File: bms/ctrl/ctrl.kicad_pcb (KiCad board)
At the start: 2 copper layers, 1 part

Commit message: BMS stuff update
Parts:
- removed the REF** at (111.9, 82.9)
- added C1: CP_1µ_100V_0805, Resistor_SMD:R_1210_3225Metric, F.Cu at (67.2, 93.3)
- added C2: CP_1µ_100V_0805, Resistor_SMD:R_1210_3225Metric, F.Cu at (67.2, 112.0)
- added C3: CP_330µ_100V_1210, localstuff:CP_Elec_19x19, F.Cu at (55.2, 104.5)
- added C4: 100nF, Capacitor_SMD:C_0603_1608Metric, F.Cu at (103.9, 106.1)
- added C5: CP_100n_50V_0603, Capacitor_SMD:C_0603_1608Metric, F.Cu at (67.0, 115.5)
- added C6: CP_100n_50V_0603, Capacitor_SMD:C_0603_1608Metric, F.Cu at (67.1, 117.4)
- added C7: CP_100n_50V_0603, Capacitor_SMD:C_0603_1608Metric, F.Cu at (67.0, 119.3)
- added C8: CP_10µ_16V_0603, Capacitor_SMD:C_0603_1608Metric, F.Cu at (108.3, 116.8)
- added D1: D_TVS_70V, localstuff:SOD-123FL, F.Cu at (66.9, 98.7)
- added D2: 1N4148, Diode_SMD:D_SOD-123, F.Cu at (105.8, 96.2)
- added D3: D_Schottky, Diode_SMD:D_SOD-123, F.Cu at (68.0, 127.2)
- added D4: D_Zener_3V3, Diode_SMD:D_SOD-123, F.Cu at (68.0, 121.5)
- added D5: 1N4148, Diode_SMD:D_SOD-123, F.Cu at (100.6, 90.5)
- added D6: 1N4148, Diode_SMD:D_SOD-123, F.Cu at (106.9, 91.0)
- added D7: 1N4148, Diode_SMD:D_SOD-123, F.Cu at (104.3, 82.3)
- added F1: Polyfuse 100V, Diode_SMD:D_SMA, F.Cu at (69.2, 104.2)
- added J1: Conn_01x02_Female, localstuff:Conn_P5.0mm_2_Lumberg, F.Cu at (48.0, 132.6)
- added J10: Conn_LEM_3, Connector_JST:JST_PH_B5B-PH-K_1x05_P2.00mm_Vertical, F.Cu at (76.6, 74.0)
- added J11: Conn_01x02_Female, Connector_PinHeader_2.54mm:PinHeader_1x02_P2.54mm_Vertical, F.Cu at (100.9, 73.6)
- added J12: Conn_01x04, Connector_PinHeader_2.54mm:PinHeader_1x04_P2.54mm_Vertical, F.Cu at (61.8, 131.0)
- added J2: Conn_01x02_Female, localstuff:Conn_P5.0mm_2_Lumberg, F.Cu at (95.5, 75.5)
- added J3: ScrewTerminal, Connector_PinHeader_2.54mm:PinHeader_1x04_P2.54mm_Vertical, F.Cu at (108.9, 73.6)
- added J4: Conn_01x06, Connector_PinHeader_2.54mm:PinHeader_1x06_P2.54mm_Vertical, F.Cu at (68.0, 86.9)
- added J5: Conn_01x04, Connector_PinHeader_2.54mm:PinHeader_1x04_P2.54mm_Vertical, F.Cu at (72.1, 74.2)
- added J6: Conn_LEM_5, Connector_JST:JST_PH_B4B-PH-K_1x04_P2.00mm_Vertical, F.Cu at (78.0, 80.2)
- added J7: Conn_01x02_Male, Connector_PinHeader_2.54mm:PinHeader_1x02_P2.54mm_Vertical, F.Cu at (64.1, 74.2)
- added J8: Conn_01x02_Female, Connector_PinHeader_2.54mm:PinHeader_1x02_P2.54mm_Vertical, F.Cu at (104.9, 73.6)
- added J9: Conn_01x03, localstuff:Conn_P5.0mm_3_Lumberg, F.Cu at (58.6, 75.1)
- added JP1: SolderJumper_3_Bridged12, Jumper:SolderJumper-3_P1.3mm_Open_Pad1.0x1.5mm, B.Cu at (109.7, 121.9)
- added JP2: SolderJumper_3_Bridged12, Jumper:SolderJumper-3_P1.3mm_Open_Pad1.0x1.5mm, B.Cu at (107.2, 121.9)
- added JP3: SolderJumper_3_Bridged12, Jumper:SolderJumper-3_P1.3mm_Open_Pad1.0x1.5mm, B.Cu at (102.2, 121.9)
- added JP4: SolderJumper_3_Bridged12, Jumper:SolderJumper-3_P1.3mm_Open_Pad1.0x1.5mm, B.Cu at (104.7, 121.9)
- added JP5: SolderJumper_3_Bridged12, Jumper:SolderJumper-3_P1.3mm_Open_Pad1.0x1.5mm, B.Cu at (99.7, 121.9)
- added JP6: OptTermination, Jumper:SolderJumper-2_P1.3mm_Open_RoundedPad1.0x1.5mm, B.Cu at (101.0, 110.0)
- added JP7: CANBUS Volt Select, Jumper:SolderJumper-3_P1.3mm_Bridged12_RoundedPad1.0x1.5mm, B.Cu at (101.1, 112.7)
- added JP8: Jumper_2_Open, Connector_PinHeader_2.54mm:PinHeader_1x02_P2.54mm_Vertical, F.Cu at (72.0, 88.8)
- added Q1: DMN2058U-7, Package_TO_SOT_SMD:SOT-23, F.Cu at (102.5, 100.5)
- added Q2: XP221P0501TR-G, Package_TO_SOT_SMD:SOT-23, F.Cu at (102.5, 95.5)
- added Q3: DMN2058U-7, Package_TO_SOT_SMD:SOT-23, F.Cu at (109.0, 100.7)
- added Q4: XP221P0501TR-G, Package_TO_SOT_SMD:SOT-23, F.Cu at (109.0, 95.5)
- added Q5: DMN2058U-7, Package_TO_SOT_SMD:SOT-23, F.Cu at (101.5, 87.3)
- added Q6: DMN2058U-7, Package_TO_SOT_SMD:SOT-23, F.Cu at (108.7, 87.9)
- added R1: R_220_0603, Resistor_SMD:R_0603_1608Metric, F.Cu at (110.0, 122.8)
- added R10: R_10k_0603, Resistor_SMD:R_0603_1608Metric, F.Cu at (71.3, 115.1)
- added R11: R_1M_0603, Resistor_SMD:R_0603_1608Metric, F.Cu at (98.7, 87.4)
- added R12: R_120_0603, Resistor_SMD:R_0603_1608Metric, F.Cu at (66.8, 89.8)
- added R13: R_1M_0603, Resistor_SMD:R_0603_1608Metric, F.Cu at (106.0, 88.0)
- added R2: R_2k2_0603, Resistor_SMD:R_0603_1608Metric, F.Cu at (99.8, 122.5)
- added R3: R_1M_0603, Resistor_SMD:R_0603_1608Metric, F.Cu at (99.7, 100.3)
- added R4: R_1M_0603, Resistor_SMD:R_0603_1608Metric, F.Cu at (102.4, 98.0)
- added R5: R_1M_0603, Resistor_SMD:R_0603_1608Metric, F.Cu at (106.1, 100.5)
- added R6: R_1M_0603, Resistor_SMD:R_0603_1608Metric, F.Cu at (109.4, 98.1)
- added R7: 120R, Resistor_SMD:R_0805_2012Metric, F.Cu at (103.8, 109.5)
- added R8: R_750k_0603, Resistor_SMD:R_0603_1608Metric, F.Cu at (67.2, 125.1)
- added R9: R_36k_0603_1, Resistor_SMD:R_0603_1608Metric, F.Cu at (67.2, 123.5)
- added REF**: OSHW-Logo2_9.8x8mm_Copper, Symbol:OSHW-Logo2_9.8x8mm_Copper, B.Cu at (82.8, 126.2)
- added REF**: OSHW-Logo2_9.8x8mm_SilkScreen, Symbol:OSHW-Logo2_9.8x8mm_SilkScreen, B.Cu at (82.8, 126.2)
- added RX1: Conn_01x02_Male, Connector_JST:JST_PH_S2B-PH-K_1x02_P2.00mm_Horizontal, F.Cu at (107.5, 129.6)
- added TP1: TestPoint, TestPoint:TestPoint_Pad_D1.5mm, F.Cu at (71.1, 111.5)
- added TX1: Conn_01x02_Male, Connector_JST:JST_PH_S2B-PH-K_1x02_P2.00mm_Horizontal, F.Cu at (100.4, 129.5)
- added U1: STH05_5V, localstuff:STH05, F.Cu at (53.8, 88.0)
- added U2: STH05_12, localstuff:STH05, F.Cu at (54.2, 120.9)
- added U3: VOS618A, Package_SO:SOP-4_4.4x2.6mm_P1.27mm, F.Cu at (104.8, 122.6)
- added U4: SN65HVD75DR, Package_SO:SOIC-8_3.9x4.9mm_P1.27mm, F.Cu at (107.7, 108.2)
- added U5: Pico, pico:RPi_Pico_SMD_TH, F.Cu at (85.9, 110.4)
- added U6: SN65HVD1050D, Package_SO:SOIC-8_3.9x4.9mm_P1.27mm, F.Cu at (103.7, 116.9)
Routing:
- net GND: track 0.00 -> 386.3 mm, vias 0 -> 27
- net +5V: track 0.00 -> 173.5 mm, vias 0 -> 9
- net +3V3: track 0.00 -> 153.3 mm, vias 0 -> 8
- net +12V: track 0.00 -> 147.4 mm, vias 0 -> 11
- net Net-(J9-Pin_1): track 0.00 -> 85.5 mm, vias 0 -> 3
- net VBAT: track 0.00 -> 85.2 mm, vias 0 -> 7
- net Net-(J9-Pin_2): track 0.00 -> 83.6 mm, vias 0 -> 5
- net ADC_BAT_I: track 0.00 -> 69.1 mm, vias 0 -> 2
- net RESET: track 0.00 -> 64.4 mm, vias 0 -> 3
- net RELAY2: track 0.00 -> 63.3 mm, vias 0 -> 2
- net RELAY1: track 0.00 -> 62.3 mm, vias 0 -> 2
- net ADC_REF_I: track 0.00 -> 59.6 mm, vias 0 -> 2
- net Net-(J3-Pin_2): track 0.00 -> 53.2 mm, vias 0 -> 5
- net I2C0_SDA: track 0.00 -> 42.5 mm, vias 0 -> 2
- net Net-(J3-Pin_3): track 0.00 -> 41.7 mm, vias 0 -> 5
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- added copper zone on B.Cu, net GND
- added copper zone on F.Cu, net GND
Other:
- board outline added: 68.8 x 65 mm
- board text added: "+"
- board text added: "+ - R Combo"
- board text added: "-"
- board text added: "12"
- board text added: "5v CAN 3.3v"
- board text added: "CAN"
- board text added: "GND"
- board text added: "GND L H"
- board text added: "MoaT comm"
- board text added: "MoaT/diyBMS battery controller V 1.0"
- board text added: "R1"
- board text added: "R2"
- board text added: "RS485"
- board text added: "RS485 term"
- board text added: "RX"
- board text added: "TX"
- board text added: "diyBMS comm"

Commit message: minor fixup
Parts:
- turned R7 to 90 degrees
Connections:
- R7 pad 1: Net-(J3-Pin_3) -> Net-(JP6-B)
- R7 pad 2: Net-(JP6-B) -> Net-(J3-Pin_3)
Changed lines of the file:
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@@
   )
   (footprint "Resistor_SMD:R_0805_2012Metric" (layer "F.Cu")
-    (at 103.8 109.4575 -90)
+    (at 103.8 109.4575 90)
     (descr "Resistor SMD 0805 (2012 Metric), square (rectangular) end terminal, IPC_7351 nominal, (Body size source: IPC-SM-782 page 72, https://www.pcb-3d.com/wordpress/wp-content/uploads/ipc-sm-782a_amendment_1_and_2.pdf), generated with kicad-footprint-generator")
     (tags "resistor")
@@
     (property "ki_keywords" "R res resistor")
     (attr smd)
-    (fp_text reference "R7" (at -0.26 1.82 90) (layer "F.SilkS")
+    (fp_text reference "R7" (at 1.2575 -1.4 90) (layer "F.SilkS")
         (effects (font (size 1 1) (thickness 0.15)))
     )
@@
     (fp_line (start 1 0.625) (end -1 0.625)
       (stroke (width 0.1) (type solid)) (layer "F.Fab"))
-    (pad "1" smd roundrect (at -0.9125 0 270) (size 1.025 1.4) (layers "F.Cu" "F.Paste" "F.Mask") (roundrect_rratio 0.243902439)
+    (pad "1" smd roundrect (at -0.9125 0 90) (size 1.025 1.4) (layers "F.Cu" "F.Paste" "F.Mask") (roundrect_rratio 0.243902439)
+      (net 29 "Net-(JP6-B)") (pintype "passive"))
+    (pad "2" smd roundrect (at 0.9125 0 90) (size 1.025 1.4) (layers "F.Cu" "F.Paste" "F.Mask") (roundrect_rratio 0.243902439)
       (net 66 "Net-(J3-Pin_3)") (pintype "passive"))
-    (pad "2" smd roundrect (at 0.9125 0 270) (size 1.025 1.4) (layers "F.Cu" "F.Paste" "F.Mask") (roundrect_rratio 0.243902439)
-      (net 29 "Net-(JP6-B)") (pintype "passive"))
     (model "${KICAD6_3DMODEL_DIR}/Resistor_SMD.3dshapes/R_0805_2012Metric.wrl"
       (offset (xyz 0 0 0))

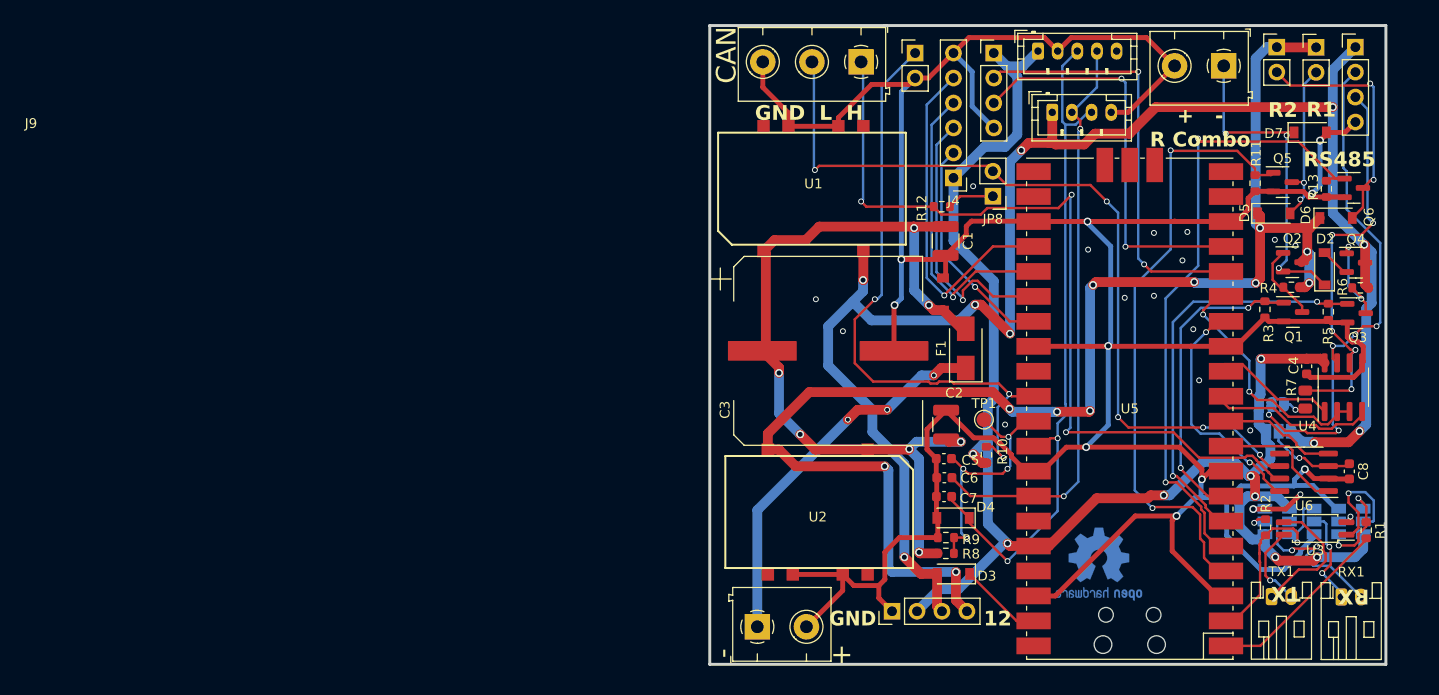
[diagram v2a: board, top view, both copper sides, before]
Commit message: Added two more config jumpers
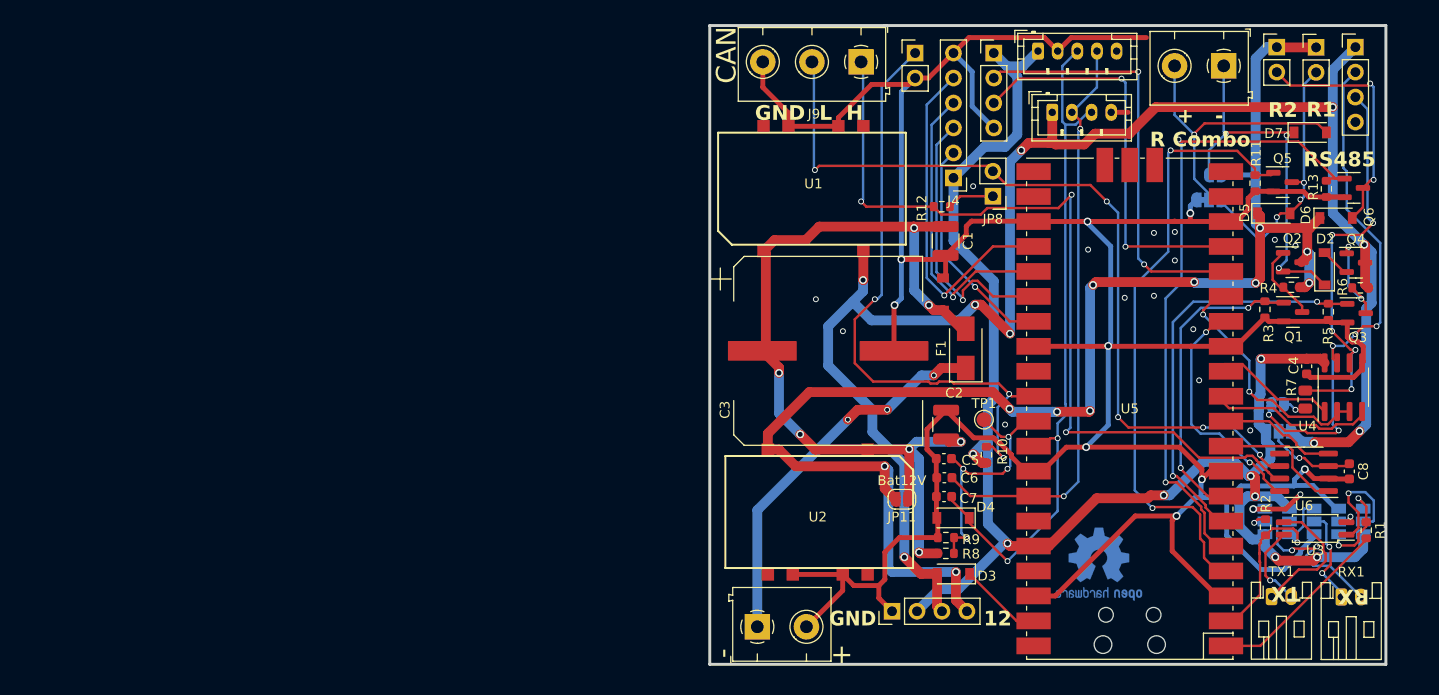
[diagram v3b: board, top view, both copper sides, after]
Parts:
- added JP10: OptTermination, Jumper:SolderJumper-2_P1.3mm_Open_RoundedPad1.0x1.5mm, B.Cu at (94.7, 86.6)
- added JP11: Bat12V, Jumper:SolderJumper-2_P1.3mm_Open_RoundedPad1.0x1.5mm, F.Cu at (62.8, 119.6)
- added JP9: Switch NC, Jumper:SolderJumper-3_P1.3mm_Bridged12_RoundedPad1.0x1.5mm, B.Cu at (94.0, 89.1)
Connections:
- net Net-(D5-A) renamed RELAY1X
- D7 pad 2: GND -> Net-(D7-A)
- J2 pad 2: GND -> Net-(D7-A)
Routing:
- net Net-(D7-A): track 0.00 -> 29.5 mm, vias 0 -> 1
- net GND: track 386.3 -> 367.3 mm, vias 27 -> 26
- net RELAY1X: track 16.8 -> 26.8 mm, vias 2 -> 3
- net +12V: track 147.4 -> 154.7 mm
- net VBAT: track 85.2 -> 90.4 mm
- net Net-(D2-K): track 34.1 -> 39.0 mm
- net RELAY2: track 63.3 -> 64.5 mm
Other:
- board text added: "See schematic!"

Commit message: BMS hardware (prev)
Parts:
- removed C3: CP_330µ_100V_1210, localstuff:CP_Elec_19x19
- removed D2, D7: 1N4148, Diode_SMD:D_SOD-123
- removed J2: Conn_01x02_Female, localstuff:Conn_P5.0mm_2_Lumberg
- removed JP10: OptTermination, Jumper:SolderJumper-2_P1.3mm_Open_RoundedPad1.0x1.5mm
- removed JP9: Switch NC, Jumper:SolderJumper-3_P1.3mm_Bridged12_RoundedPad1.0x1.5mm
- removed Q1, Q3: DMN2058U-7, Package_TO_SOT_SMD:SOT-23
- removed Q2, Q4: XP221P0501TR-G, Package_TO_SOT_SMD:SOT-23
- removed R3, R4, R5, R6: R_1M_0603, Resistor_SMD:R_0603_1608Metric
- added D8: LED_red, LED_SMD:LED_0805_2012Metric, F.Cu at (69.9, 91.4)
- added D9: LED_green, LED_SMD:LED_0805_2012Metric, F.Cu at (67.6, 91.4)
- added JP12: 24V, Jumper:SolderJumper-2_P1.3mm_Open_RoundedPad1.0x1.5mm, B.Cu at (68.4, 111.4)
- added JP13: 12V, Jumper:SolderJumper-2_P1.3mm_Open_RoundedPad1.0x1.5mm, B.Cu at (64.9, 111.4)
- added R14: R_750k_0603, Resistor_SMD:R_0603_1608Metric, F.Cu at (68.5, 111.4)
- added R15: R_750k_0603, Resistor_SMD:R_0603_1608Metric, F.Cu at (65.1, 111.4)
- added R16: R_560_0603, Resistor_SMD:R_0603_1608Metric, F.Cu at (62.4, 89.2)
- added R17: R_510_0603, Resistor_SMD:R_0603_1608Metric, F.Cu at (64.2, 89.2)
- J11: footprint Connector_PinHeader_2.54mm:PinHeader_1x02_P2.54mm_Vertical -> Connector_JST:JST_PH_S2B-PH-K_1x02_P2.00mm_Horizontal
- J8: footprint Connector_PinHeader_2.54mm:PinHeader_1x02_P2.54mm_Vertical -> localstuff:Conn_P5.0mm_2_Lumberg
- JP8: value Jumper_2_Open -> 24V; footprint Connector_PinHeader_2.54mm:PinHeader_1x02_P2.54mm_Vertical -> Jumper:SolderJumper-2_P1.3mm_Open_RoundedPad1.0x1.5mm; moved to B.Cu
- moved R12 41.9 mm to (100.5, 114.8), turned to 90 degrees
- moved JP8 34.2 mm to (96.3, 112.8), turned to 0 degrees
- moved J8 9.76 mm to (95.3, 75.4), turned to 180 degrees
- moved U2 8.59 mm to (52.4, 112.5), turned to 90 degrees
- moved J12 8.28 mm to (69.7, 133.3), turned to -90 degrees
- moved J3 7.60 mm to (108.9, 81.2), turned to 180 degrees
- moved C2 6.70 mm to (60.8, 113.8)
- moved C1 6.28 mm to (61.1, 94.8), turned to 90 degrees
- moved J11 5.37 mm to (103.5, 78.3), turned to 180 degrees
- moved U1 3.84 mm to (52.4, 91.6), turned to 90 degrees
- moved J1 2.26 mm to (50.3, 132.6)
- moved C8 1.82 mm to (110.1, 116.7)
- moved U6 1.63 mm to (105.3, 116.9)
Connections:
- net RELAY1X renamed Net-(D5-A)
- F1 pad 1: Net-(J1-Pin_1) -> Net-(J1-Pin_2)
- J1 pad 1: Net-(J1-Pin_1) -> GND
- J1 pad 2: GND -> Net-(J1-Pin_2)
- J12 pad 1: GND -> +12V
- J12 pad 2: +3V3 -> +5V
- J12 pad 3: +5V -> +3V3
- J12 pad 4: +12V -> GND
- J3 pad 1: +5V -> GND
- J3 pad 4: GND -> +5V
- JP6 pad 1: Net-(J3-Pin_2) -> Net-(J3-Pin_3)
- JP8 pad 1: Net-(JP8-A) -> Net-(J9-Pin_2)
- JP8 pad 2: Net-(J9-Pin_2) -> Net-(R12-Pad2)
- R12 pad 2: Net-(JP8-A) -> Net-(R12-Pad2)
- R7 pad 2: Net-(J3-Pin_3) -> Net-(J3-Pin_2)
- U4 pad 6: Net-(J3-Pin_3) -> Net-(J3-Pin_2)
- U4 pad 7: Net-(J3-Pin_2) -> Net-(J3-Pin_3)
- U5 pad 21: unconnected-(U5-GPIO16) -> LED_RED
- U5 pad 22: unconnected-(U5-GPIO17) -> LED_GREEN
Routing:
- net Net-(J1-Pin_2): track 0.00 -> 42.0 mm, vias 0 -> 1
- net RELAY3L: track 41.0 -> 0.00 mm, vias 2 -> 0
- net Net-(J1-Pin_1): track 39.2 -> 0.00 mm, vias 3 -> 0
- net Net-(D2-K): track 39.0 -> 0.00 mm, vias 3 -> 0
- net VBAT: track 90.4 -> 55.5 mm, vias 7 -> 3
- net RELAY3H: track 30.9 -> 0.00 mm, vias 2 -> 0
- net Net-(D7-A): track 29.5 -> 0.00 mm, vias 1 -> 0
- net +12V: track 154.7 -> 136.6 mm, vias 11 -> 9
- net +3V3: track 153.3 -> 168.6 mm, vias 8 -> 10
- net RELAY2: track 64.5 -> 78.6 mm
- net Net-(J3-Pin_3): track 41.7 -> 53.8 mm
- net +5V: track 173.5 -> 185.1 mm, vias 9 -> 8
- net Net-(J3-Pin_2): track 53.2 -> 41.9 mm
- net LED_GREEN: track 0.00 -> 10.9 mm
- net Net-(Q3-D): track 9.74 -> 0.00 mm, vias 2 -> 0
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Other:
- board size 68.8 x 65 mm -> 67 x 65 mm
- board text added: "- + R Combo"
- board text added: "GND CAN:L H"
- board text added: "MoaT/diyBMS battery controller"
- board text added: "V1.2"
- board text added: "open: 48V"
- board text removed: "+ - R Combo"
- board text removed: "GND L H"
- board text removed: "MoaT/diyBMS battery controller V 1.0"

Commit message: Old check-in: ctrl
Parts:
- removed C1: CP_1µ_100V_0805, Resistor_SMD:R_1210_3225Metric
- removed C4: 100nF, Capacitor_SMD:C_0603_1608Metric
- removed D3: D_Schottky, Diode_SMD:D_SOD-123
- removed D6: 1N4148, Diode_SMD:D_SOD-123
- removed D8: LED_red, LED_SMD:LED_0805_2012Metric
- removed D9: LED_green, LED_SMD:LED_0805_2012Metric
- removed J11: Conn_01x02_Female, Connector_JST:JST_PH_S2B-PH-K_1x02_P2.00mm_Horizontal
- removed J3: ScrewTerminal, Connector_PinHeader_2.54mm:PinHeader_1x04_P2.54mm_Vertical
- removed J7: Conn_01x02_Male, Connector_PinHeader_2.54mm:PinHeader_1x02_P2.54mm_Vertical
- removed J9: Conn_01x03, localstuff:Conn_P5.0mm_3_Lumberg
- removed JP6: OptTermination, Jumper:SolderJumper-2_P1.3mm_Open_RoundedPad1.0x1.5mm
- removed JP7: CANBUS Volt Select, Jumper:SolderJumper-3_P1.3mm_Bridged12_RoundedPad1.0x1.5mm
- removed JP8: 24V, Jumper:SolderJumper-2_P1.3mm_Open_RoundedPad1.0x1.5mm
- removed R10: R_10k_0603, Resistor_SMD:R_0603_1608Metric
- removed R12: R_120_0603, Resistor_SMD:R_0603_1608Metric
- removed R17: R_510_0603, Resistor_SMD:R_0603_1608Metric
- removed R7: 120R, Resistor_SMD:R_0805_2012Metric
- removed U5: Pico, pico:RPi_Pico_SMD_TH
- removed U6: SN65HVD1050D, Package_SO:SOIC-8_3.9x4.9mm_P1.27mm
- added C3: CP_22m_16V, Capacitor_THT:CP_Radial_D22.0mm_P10.00mm_SnapIn, F.Cu at (84.4, 103.9)
- added R3: R_5k1_0603, Resistor_SMD:R_0603_1608Metric, F.Cu at (61.6, 92.6)
- added R4: R_5k1_0603, Resistor_SMD:R_0603_1608Metric, F.Cu at (64.7, 92.6)
- added REF**: MountingHole_3.2mm_M3, MountingHole:MountingHole_3.2mm_M3, F.Cu at (98.1, 75.3)
- added REF**: MountingHole_3.2mm_M3, MountingHole:MountingHole_3.2mm_M3, F.Cu at (98.1, 119.9)
- added REF**: MountingHole_3.2mm_M3, MountingHole:MountingHole_3.2mm_M3, F.Cu at (49.0, 119.9)
- added REF**: MountingHole_3.2mm_M3, MountingHole:MountingHole_3.2mm_M3, F.Cu at (48.7, 75.4)
- added U7: tiny2040, localstuff:tiny2040, F.Cu at (68.3, 80.8)
- C8: value CP_10µ_16V_0603 -> CP_100n_50V_0603
- F1: value Polyfuse 100V -> Fuse; footprint Diode_SMD:D_SMA -> Fuse:Fuseholder_Cylinder-5x20mm_Stelvio-Kontek_PTF78_Horizontal_Open
- R16: value R_560_0603 -> R_22_0603
- U1: value STH05_5V -> MCP3428; footprint localstuff:STH05 -> Package_SO:SOIC-14_3.9x8.7mm_P1.27mm
- U2: value STH05_12 -> MCP3426-xMC; footprint localstuff:STH05 -> Package_DFN_QFN:DFN-8-1EP_3x2mm_P0.5mm_EP1.75x1.45mm
- U3: footprint Package_SO:SOP-4_4.4x2.6mm_P1.27mm -> Package_SO:SO-4_4.4x4.3mm_P2.54mm
- U4: value SN65HVD75DR -> TSR_1-48150WI; footprint Package_SO:SOIC-8_3.9x4.9mm_P1.27mm -> localstuff:TSR_1-48150WI
- moved C8 59.3 mm to (56.9, 90.6), turned to 180 degrees
- moved U4 46.5 mm to (61.5, 102.8), turned to -90 degrees
- moved J8 45.4 mm to (86.8, 120.0), turned to 0 degrees
- moved D4 44.1 mm to (49.0, 81.7), turned to 90 degrees
- moved R1 41.9 mm to (73.2, 102.8), turned to 0 degrees
- moved JP1 41.8 mm to (72.3, 103.1), turned to 0 degrees
- moved REF** 40.4 mm to (51.1, 101.1) (x2)
- moved R8 39.8 mm to (53.6, 87.7), turned to 90 degrees
- moved R9 38.9 mm to (51.9, 87.7), turned to -90 degrees
- moved JP2 38.5 mm to (72.3, 105.6), turned to 0 degrees
- moved C7 36.9 mm to (53.5, 85.0), turned to 0 degrees
- moved JP4 35.2 mm to (72.3, 108.1), turned to 0 degrees
- moved U3 35.0 mm to (73.0, 108.0), turned to -90 degrees
- moved C6 34.0 mm to (56.7, 85.0)
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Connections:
- C8 pad 1: Net-(JP7-C) -> +3V3
- D4 pad 1: ADC_BAT_I -> ADC_BAT_U
- J12 pad 1: +12V -> GND
- J12 pad 2: +5V -> +3V3
- J12 pad 3: +3V3 -> +5V
- J12 pad 4: GND -> +12V
- J4 pad 1: +3V3 -> GND
- J4 pad 2: IO1 -> IO4
- J4 pad 3: IO2 -> IO3
- J4 pad 4: IO3 -> IO2
- J4 pad 5: IO4 -> IO1
- J4 pad 6: GND -> +3V3
- J5 pad 1: +3V3 -> GND
- J5 pad 2: I2C0_SDA -> I2C0_SCL
- J5 pad 3: I2C0_SCL -> I2C0_SDA
- J5 pad 4: GND -> +3V3
- Q6 pad 3: Net-(D6-A) -> Net-(Q6-D)
- R16 pad 1: +3V3 -> Net-(Q6-D)
- U1 pad 1: VBAT -> ADC_BAT_I
- U1 pad 10: unconnected-(U1-Enable) -> GND
- U1 pad 5: +5V -> GND
- U1 pad 6: unconnected-(U1-Trim) -> +3V3
- U1 pad 7: GND -> I2C0_SDA
- U2 pad 1: VBAT -> ADC_BAT_I
- U2 pad 5: +12V -> I2C0_SCL
- U2 pad 6: unconnected-(U2-Trim) -> GND
- U2 pad 7: GND -> ADC_BAT_U
- U4 pad 1: RS485_RX -> VBAT
- U4 pad 2: RS485_ENA -> GND
- U4 pad 3: RS485_ENA -> +12V
- U4 pad 4: RS485_TX -> Net-(U4-CASE_PIN)
- U4 pad 5: GND -> Net-(U4-CASE_PIN)
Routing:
- net GND: track 358.4 -> 37.4 mm, vias 26 -> 46
- net +5V: track 185.1 -> 68.4 mm, vias 8 -> 0
- net Net-(J9-Pin_1): track 90.3 -> 0.00 mm, vias 3 -> 0
- net Net-(J9-Pin_2): track 89.8 -> 0.00 mm, vias 5 -> 0
- net RESET: track 59.3 -> 0.00 mm, vias 3 -> 0
- net Net-(J3-Pin_3): track 53.8 -> 0.00 mm, vias 5 -> 0
- net +12V: track 136.6 -> 87.5 mm, vias 9 -> 0
- net Net-(J3-Pin_2): track 41.9 -> 0.00 mm, vias 5 -> 0
- net RELAY2: track 78.6 -> 37.7 mm, vias 2 -> 1
- net ADC_BAT_I: track 69.8 -> 28.9 mm, vias 2 -> 1
- net ADC_REF_I: track 60.0 -> 21.3 mm
- net RELAY1: track 71.0 -> 32.8 mm, vias 2 -> 1
- net Net-(J1-Pin_2): track 42.0 -> 13.3 mm, vias 1 -> 0
- net RX_BAT: track 22.6 -> 50.2 mm
- net CAN_S: track 26.5 -> 0.00 mm, vias 2 -> 0
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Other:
- board size 67 x 65 mm -> 56.8 x 52.4 mm
- board text added: "- + Relais"
- board text added: "V2.1"
- board text removed: "- + R Combo"
- board text removed: "5v CAN 3.3v"
- board text removed: "CAN"
- board text removed: "GND CAN:L H"
- board text removed: "R1"
- board text removed: "R2"
- board text removed: "RS485"
- board text removed: "RS485 term"
- board text removed: "V1.2"
- board text removed: "open: 48V"
